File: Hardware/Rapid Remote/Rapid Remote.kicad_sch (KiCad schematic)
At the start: 38 parts, among them U2 ESP32-C3-MINI-1-N4, U3 MIC5504-3.3YM5, U3 WS4518D, U6 XB6042I2SV

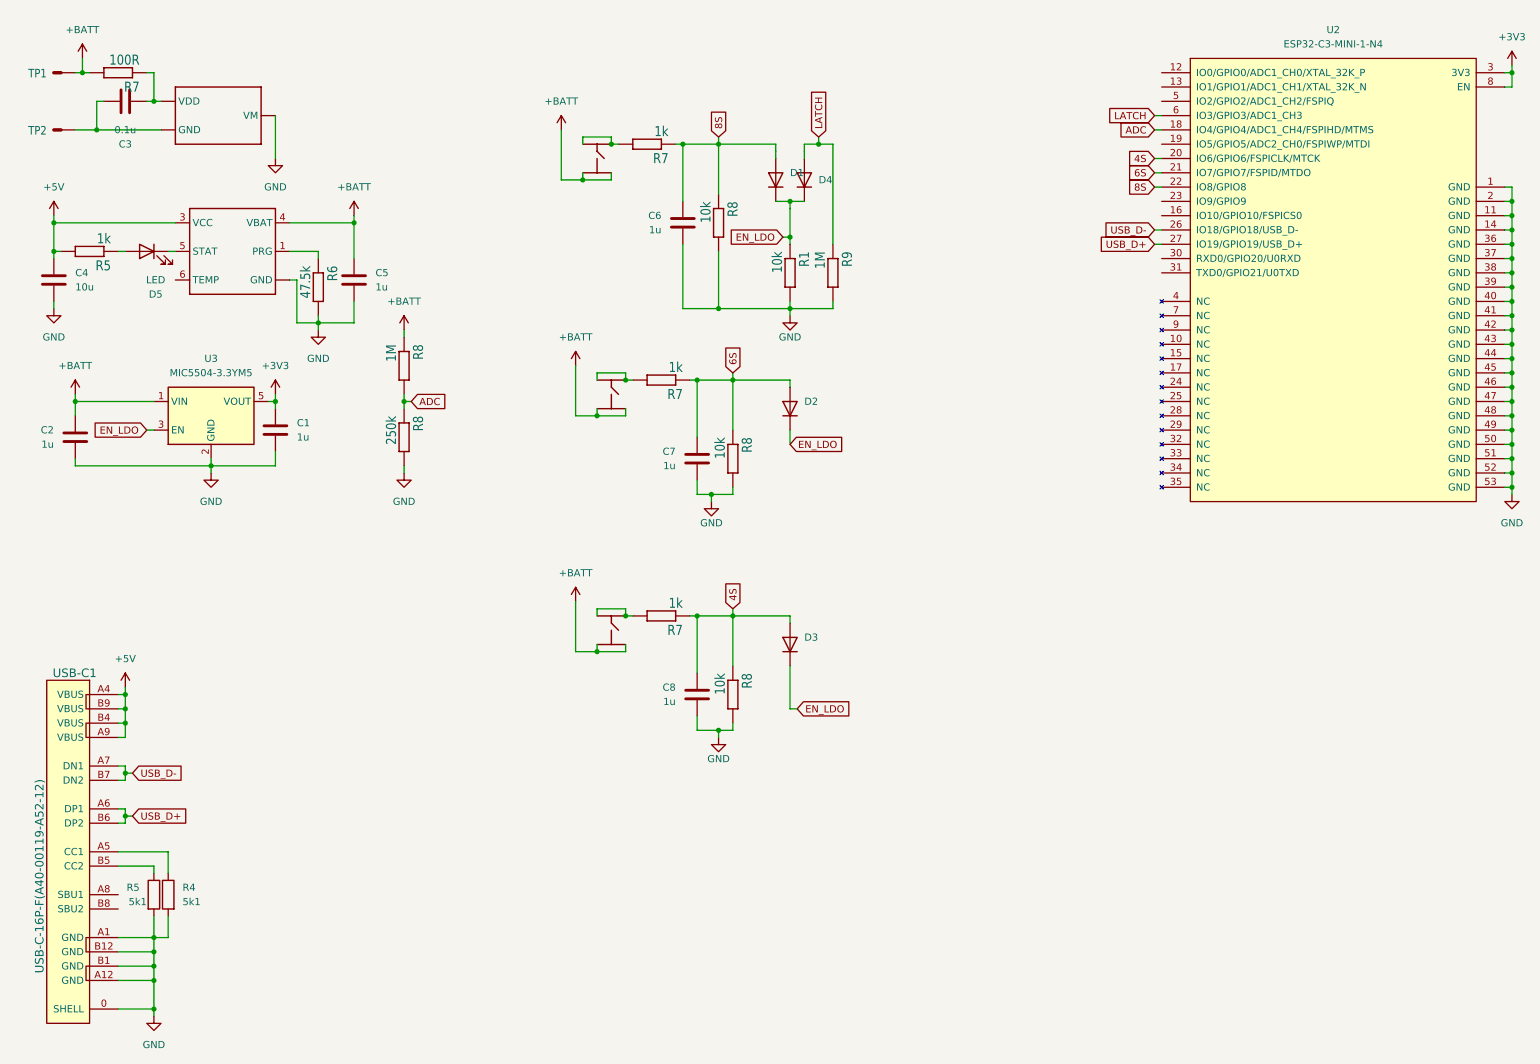
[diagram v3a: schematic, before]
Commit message: added battery and code for remote
Added a cr2032 battery for power and finished the layout and programming of the remote
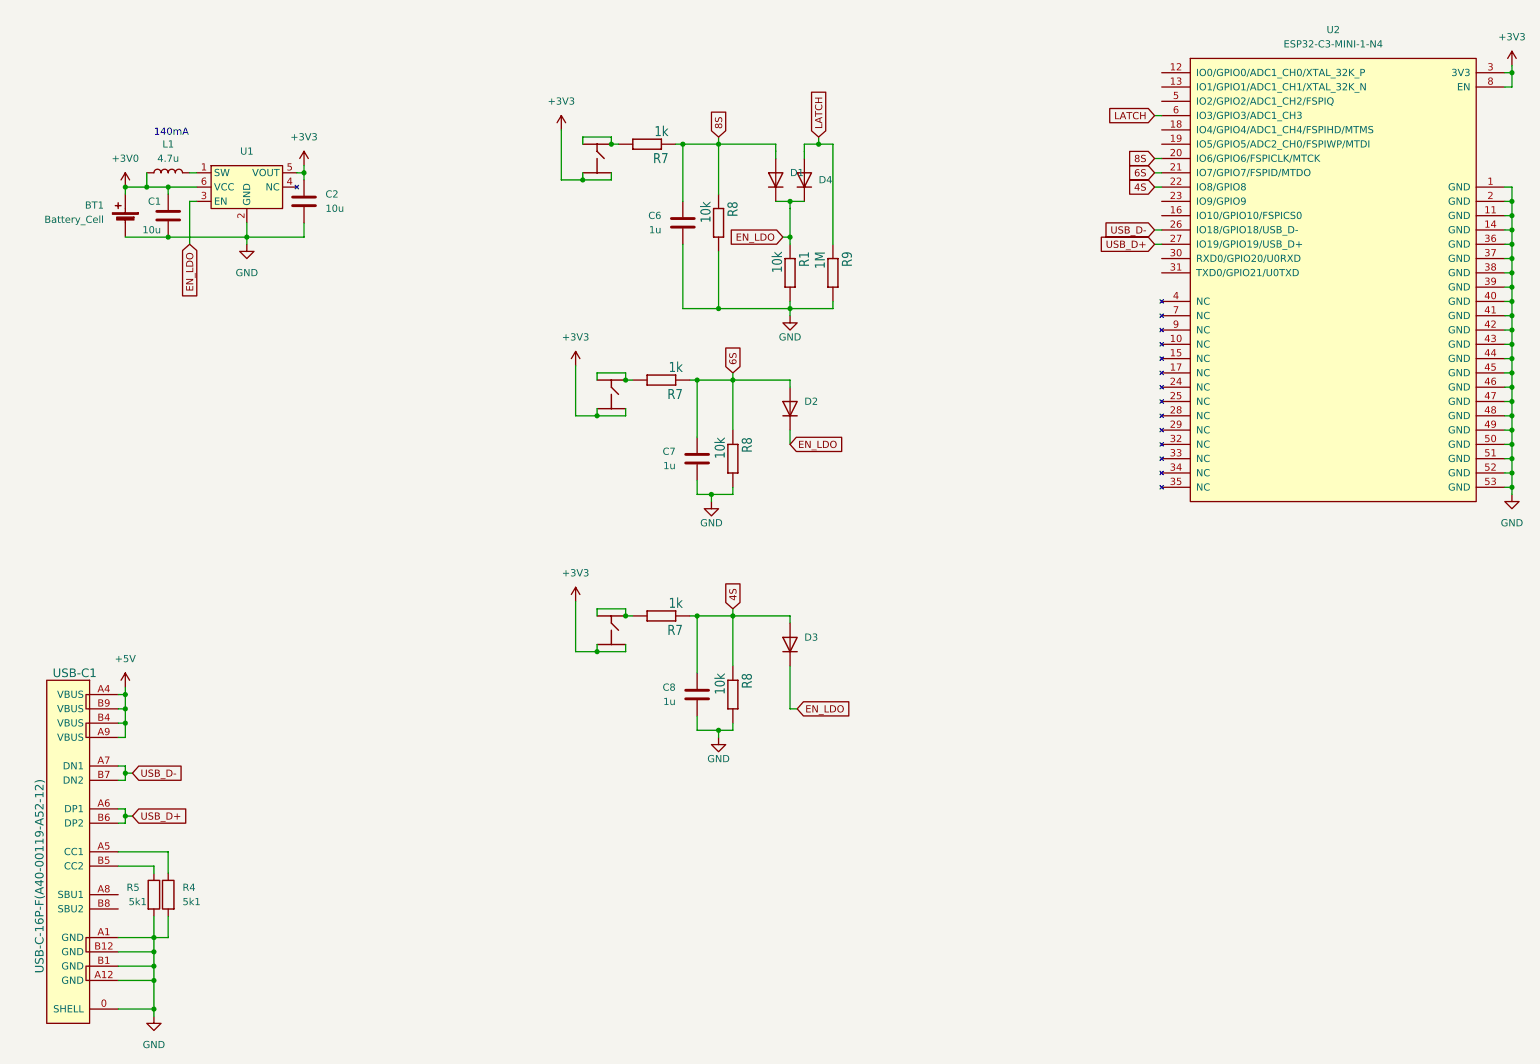
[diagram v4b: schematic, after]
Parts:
- removed C3: 0.1u, Capacitor_SMD:C_0402_1005Metric, symbol Device:C
- removed C4: 10u, Capacitor_SMD:C_0402_1005Metric, symbol Device:C
- removed C5: 1u, Capacitor_SMD:C_0402_1005Metric, symbol Device:C
- removed D5: LED, LED_SMD:LED_0402_1005Metric, symbol Device:LED
- removed R5: 1k, Resistor_SMD:R_0402_1005Metric, symbol picoclick_c3_v1.1-eagle-import:moekoe_rcl_R0402
- removed R6: 47.5k, Resistor_SMD:R_0402_1005Metric, symbol picoclick_c3_v1.1-eagle-import:moekoe_rcl_R0402
- removed R7: 100R, Resistor_SMD:R_0402_1005Metric, symbol picoclick_c3_v1.1-eagle-import:moekoe_rcl_R0402
- removed R8: 250k, Resistor_SMD:R_0402_1005Metric, symbol picoclick_c3_v1.1-eagle-import:moekoe_rcl_R0402
- removed R8: 1M, Resistor_SMD:R_0402_1005Metric, symbol picoclick_c3_v1.1-eagle-import:moekoe_rcl_R0402
- removed TP1, TP2: TP/SP-1.5X2.0, Personal:SOLDERPAD_1.5X2.0, symbol picoclick_c3_v1.1-eagle-import:iml_elc_TP/SP-1.5X2.0
- removed U3: WS4518D, Personal:DFN-6, symbol picoclick_c3_v1.1-eagle-import:moekoe_ics_WS4518D
- removed U3: MIC5504-3.3YM5, Package_TO_SOT_SMD:SOT-23-5, symbol Regulator_Linear:MIC5504-3.3YM5
- removed U6: XB6042I2SV, Personal:TDFN4, symbol picoclick_c3_v1.1-eagle-import:moekoe_XB6042I2SV
- added BT1: Battery_Cell, personal:MY-2032-04, symbol Device:Battery_Cell
- added L1: 4.7u, Inductor_SMD:L_0603_1608Metric, symbol Device:L
- added U1: ~, Package_TO_SOT_SMD:SOT-23-6, symbol remote:SGM6603-3.3Y
- C1, C2: value 1u -> 10u
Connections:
- net +BATT is gone; now on net +3V3: C2.1, s4.P3 (3), s4.P4 (4), s6.P3 (3), s6.P4 (4), s8.P3 (3), s8.P4 (4)
- net +3V3: now also U1.5 (VOUT); no longer C1.1
- net 4S: now also U2.22 (IO8/GPIO8); no longer U2.20 (IO6/GPIO6/FSPICLK/MTCK)
- net 8S: now also U2.20 (IO6/GPIO6/FSPICLK/MTCK); no longer U2.22 (IO8/GPIO8)
- net EN_LDO: now also U1.3 (EN)
- net GND: now also BT1.2 (-), U1.2 (GND)
- net ADC: no longer names the net of U2.18 (IO4/GPIO4/ADC1_CH4/FSPIHD/MTMS)
- new net: L1.2, U1.1 (SW)
- new net +3V0: BT1.1 (+), C1.1, L1.1, U1.6 (VCC)
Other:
- note added: "140mA"

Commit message: changed to 0603 capacitors
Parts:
- C1, C2: footprint Capacitor_SMD:C_0402_1005Metric -> Capacitor_SMD:C_0603_1608Metric
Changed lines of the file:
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@@
       (effects (font (size 1.27 1.27)) (justify left))
     )
-    (property "Footprint" "Capacitor_SMD:C_0402_1005Metric" (at 63.1952 49.53 0)
+    (property "Footprint" "Capacitor_SMD:C_0603_1608Metric" (at 63.1952 49.53 0)
       (effects (font (size 1.27 1.27)) hide)
     )
@@
       (effects (font (size 1.27 1.27)) (justify left))
     )
-    (property "Footprint" "Capacitor_SMD:C_0402_1005Metric" (at 37.1348 52.07 0)
-      (effects (font (size 1.27 1.27)) hide)
-    )
+    (property "Footprint" "Capacitor_SMD:C_0603_1608Metric" (at 37.1348 52.07 0)
+      (effects (font (size 1.27 1.27)) hide)
+    )

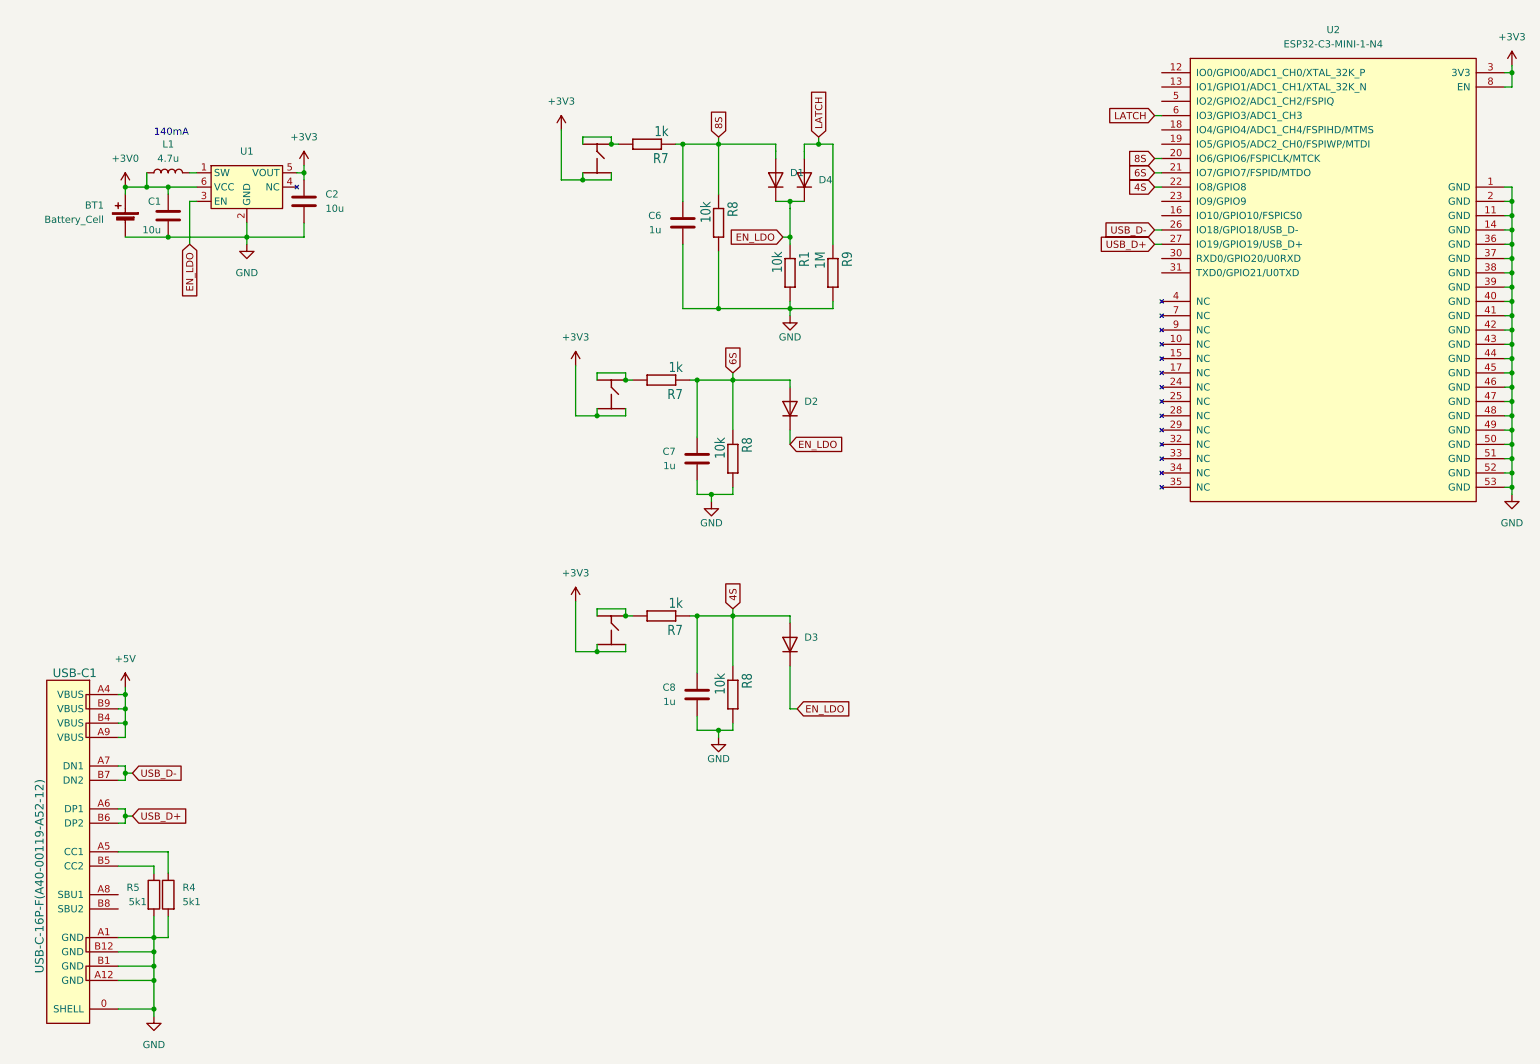
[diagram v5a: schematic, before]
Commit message: updated remote to rev C
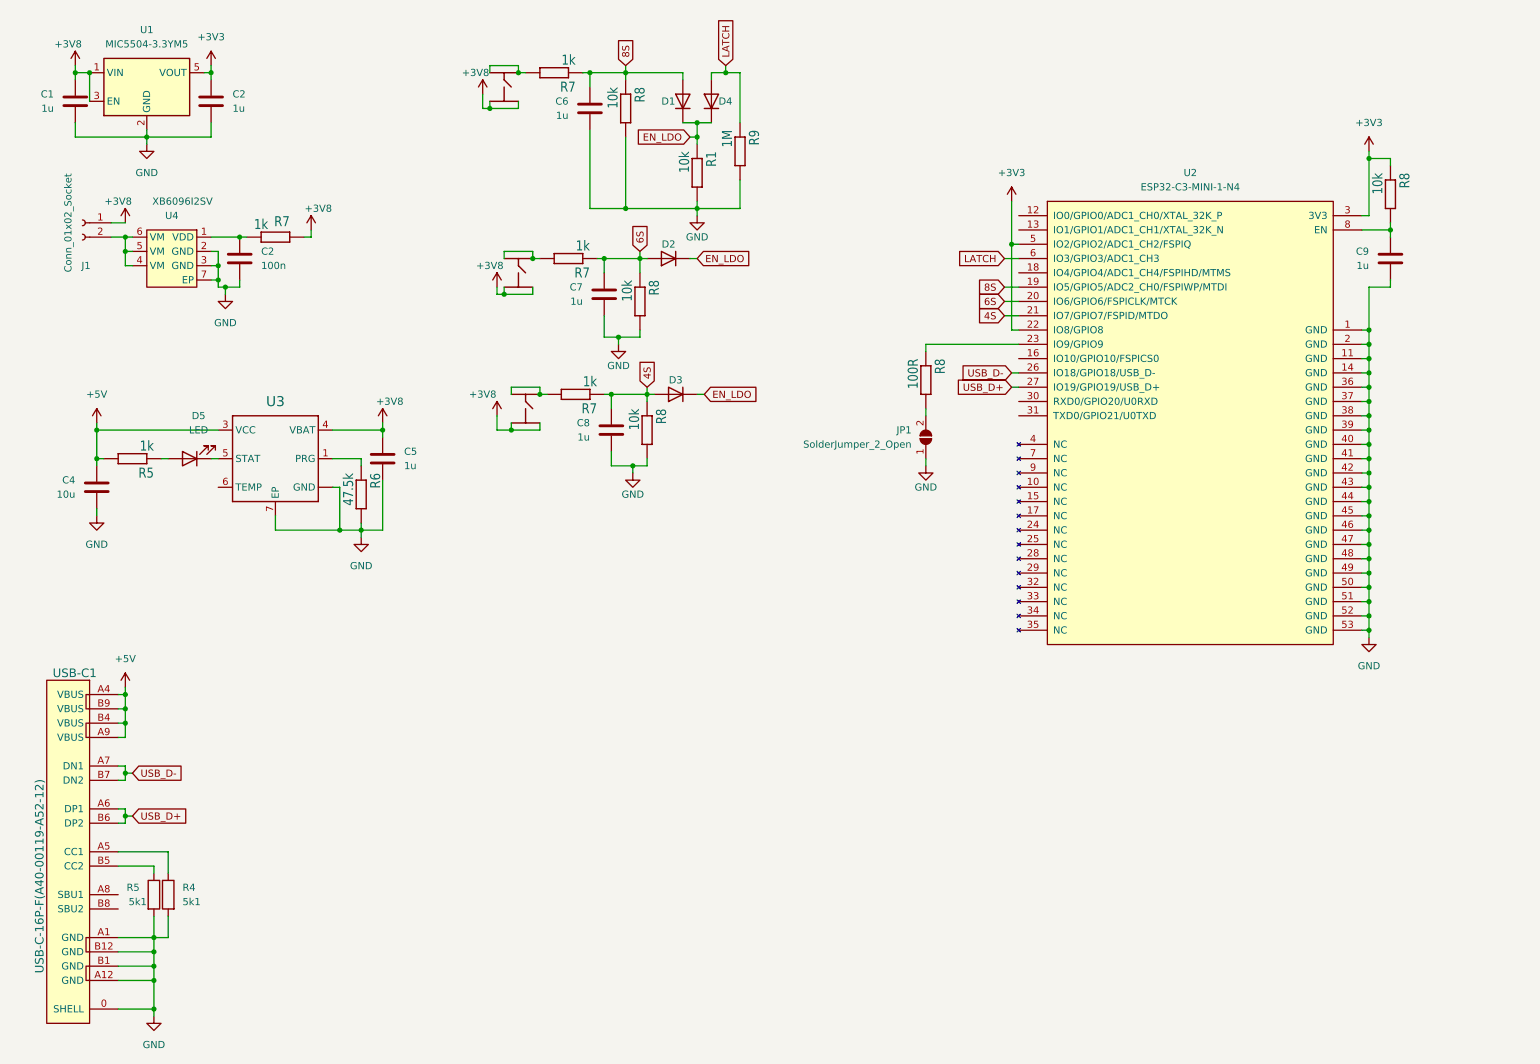
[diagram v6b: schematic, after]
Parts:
- removed BT1: Battery_Cell, personal:MY-2032-04, symbol Device:Battery_Cell
- removed C2: 10u, Capacitor_SMD:C_0603_1608Metric, symbol Device:C
- removed L1: 4.7u, Inductor_SMD:L_0603_1608Metric, symbol Device:L
- removed U1: ~, Package_TO_SOT_SMD:SOT-23-6, symbol remote:SGM6603-3.3Y
- added C2: 100n, Capacitor_SMD:C_0603_1608Metric, symbol Device:C
- added C2, C5, C9: 1u, Capacitor_SMD:C_0603_1608Metric, symbol Device:C
- added C4: 10u, Capacitor_SMD:C_0603_1608Metric, symbol Device:C
- added D5: LED, LED_SMD:LED_0603_1608Metric, symbol Device:LED
- added J1: Conn_01x02_Socket, Connector_JST:JST_PH_B2B-PH-K_1x02_P2.00mm_Vertical, symbol Connector:Conn_01x02_Socket
- added JP1: SolderJumper_2_Open, Jumper:SolderJumper-2_P1.3mm_Open_RoundedPad1.0x1.5mm, symbol Jumper:SolderJumper_2_Open
- added R5, R7: 1k, Resistor_SMD:R_0603_1608Metric, symbol picoclick_c3_v1.1-eagle-import:moekoe_rcl_R0402
- added R6: 47.5k, Resistor_SMD:R_0603_1608Metric, symbol picoclick_c3_v1.1-eagle-import:moekoe_rcl_R0402
- added R8: 10k, Resistor_SMD:R_0603_1608Metric, symbol picoclick_c3_v1.1-eagle-import:moekoe_rcl_R0402
- added R8: 100R, Resistor_SMD:R_0603_1608Metric, symbol picoclick_c3_v1.1-eagle-import:moekoe_rcl_R0402
- added U1: MIC5504-3.3YM5, Package_TO_SOT_SMD:SOT-23-5, symbol Regulator_Linear:MIC5504-3.3YM5
- added U3: WS4518D, Package_DFN_QFN:DFN-6-1EP_2x2mm_P0.65mm_EP1x1.6mm, symbol picoclick_c3_v1.1-eagle-import:moekoe_ics_WS4518D
- added U4: XB6096I2SV, Package_DFN_QFN:DFN-6-1EP_2x2mm_P0.65mm_EP1x1.6mm, symbol personal2:XB6096I2SV_
- C1: value 10u -> 1u
- C6, C7, C8: footprint Capacitor_SMD:C_0402_1005Metric -> Capacitor_SMD:C_0603_1608Metric
- R1, R4, R5, R7, R8, R9: footprint Resistor_SMD:R_0402_1005Metric -> Resistor_SMD:R_0603_1608Metric
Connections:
- net +3V3: now also U2.22 (IO8/GPIO8), U2.5 (IO2/GPIO2/ADC1_CH2/FSPIQ), C2.1, R8.1, U1.5 (VOUT); no longer U2.8 (EN), s4.P3 (3), s4.P4 (4), s6.P3 (3), s6.P4 (4), s8.P3 (3), s8.P4 (4)
- net +5V: now also C4.1, R5.2, U3.3 (VCC)
- net 4S: now also U2.21 (IO7/GPIO7/FSPID/MTDO); no longer U2.22 (IO8/GPIO8)
- net 6S: now also U2.20 (IO6/GPIO6/FSPICLK/MTCK); no longer U2.21 (IO7/GPIO7/FSPID/MTDO)
- net 8S: now also U2.19 (IO5/GPIO5/ADC2_CH0/FSPIWP/MTDI); no longer U2.20 (IO6/GPIO6/FSPICLK/MTCK)
- net GND: now also C2.2, C2.2, C4.2, C5.2, C9.2, JP1.1 (A), R6.2, U1.2 (GND), U3.2 (GND), U3.7 (EP), U3.EXP (GND), U4.2 (GND), U4.3 (GND), U4.7 (EP)
- net at U2.23 (IO9/GPIO9): now also R8.1
- net +3V0 renamed +3V8
- net +3V8: now also s4.P3 (3), s4.P4 (4), s6.P3 (3), s6.P4 (4), s8.P3 (3), s8.P4 (4), C5.1, J1.1 (Pin_1), R7.2, U1.1 (VIN), U1.3 (EN), U3.4 (VBAT)
- new net: C2.1, R7.1, U4.1 (VDD)
- new net: D5.2 (A), R5.1
- new net: J1.2 (Pin_2), U4.4 (VM), U4.5 (VM), U4.6 (VM)
- new net: D5.1 (K), U3.5 (STAT)
- new net: R6.1, U3.1 (PRG)
- new net: JP1.2 (B), R8.2
- new net: C9.1, R8.2, U2.8 (EN)
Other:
- note removed: "140mA"
- moved on the sheet: C6, C7, C8, D1, D2, D3, D4, R1, R7, R8, R9, U2

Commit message: rev c of remote and cad
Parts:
- added H1, H2, H3: MountingHole, MountingHole:MountingHole_3.2mm_M3, symbol Mechanical:MountingHole
- J1: footprint Connector_JST:JST_PH_B2B-PH-K_1x02_P2.00mm_Vertical -> Connector_JST:JST_PH_S2B-PH-SM4-TB_1x02-1MP_P2.00mm_Horizontal
